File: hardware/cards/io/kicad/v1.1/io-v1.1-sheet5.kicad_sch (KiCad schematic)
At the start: 8 parts, among them IC10 74*273, IC5 74*138, IC7 74*00, IC8 74*06

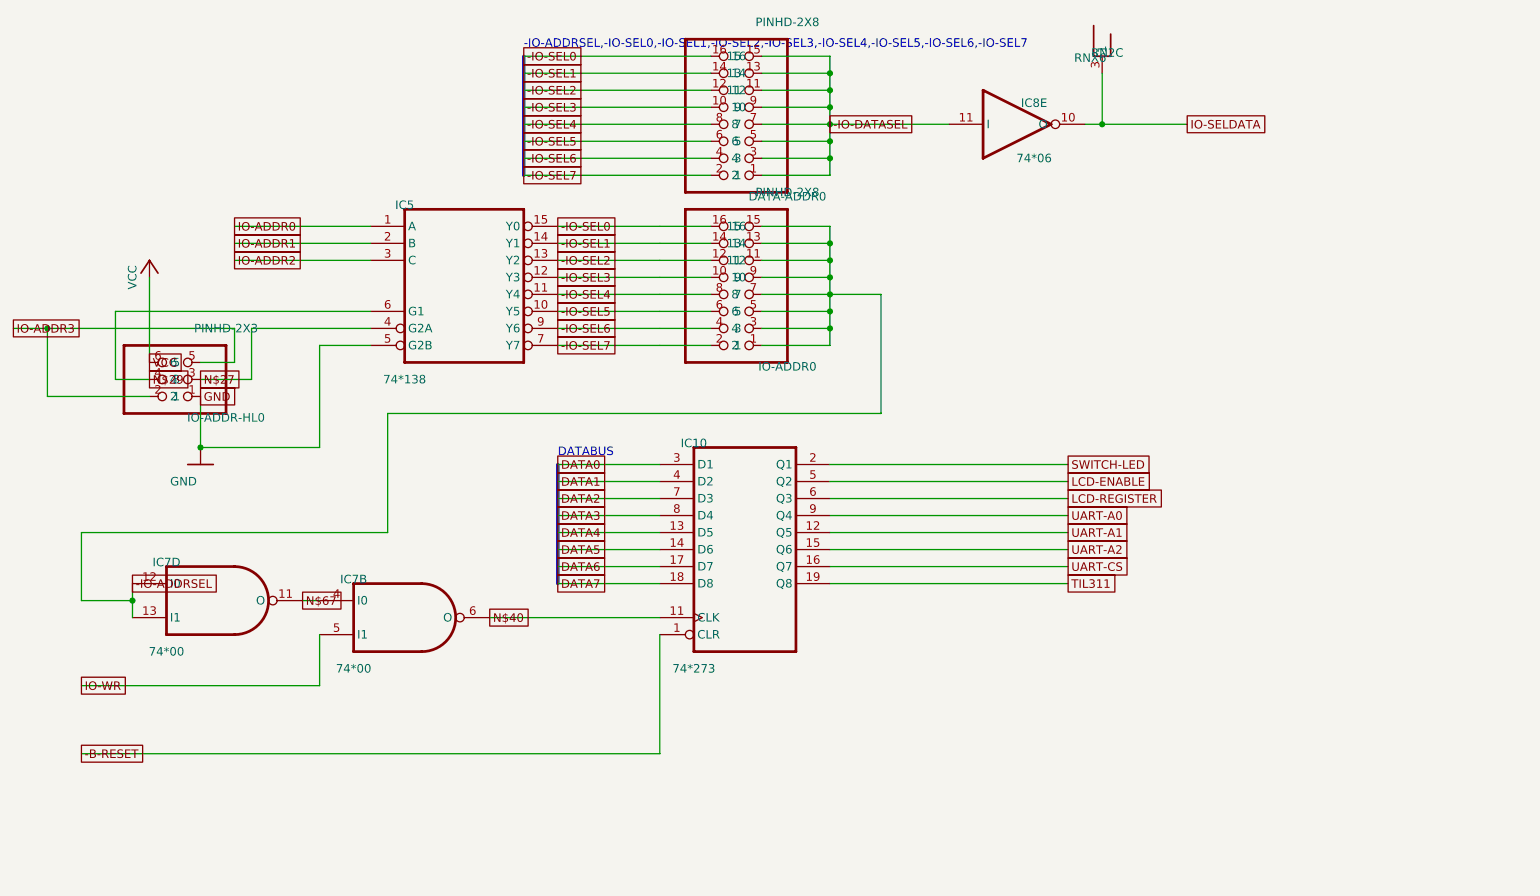
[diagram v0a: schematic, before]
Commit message: fix(kicad): readable converted schematics - overlaps 42,847 -> 3,147, nothing off the frame; CF sheet 0 overlaps
- tools/kicad/sch_overlaps.py: calibrated readability check (text/text, text/body, text/line, off frame/title block)
- eagle_sch_to_kicad.py: fields placed from Eagle's smashed attributes or the symbol's >NAME/>VALUE with Eagle's align,
  size and ratio, readable angles; fields Eagle never shows hidden (FABC96R shows only its pin name); pin numbers hidden
  where every Eagle pin hides them; Eagle-hidden layers dropped (the stray SpiceOrder text); labels on their own wires,
  converter labels only where KiCad needs them; rotate-then-mirror fixed for MR90/MR270 in pin_world/no-connects;
  each sheet on the smallest page that holds it, centred clear of the title block
- finish_board.py: stable footprint-library choice (DRC counts no longer vary run to run)
- all 37 projects regenerated: netlist proofs unchanged (34 MATCH, 2 schematic-only, video Fusion export MISMATCH as
  before); DRC same or better; ERC up (loose wire ends onto graphic buses no longer hidden by labels; explained per README)
- CF card: gate names off the gate bodies, U3 clear of its title, 5.08 mm connector pins; rebuilt: DRC 0/0, proof MATCH
- schematic PDFs regenerated (tools/sch_to_pdf.py, 37/37)

Co-Authored-By: Claude Opus 5.5 <noreply@anthropic.com>
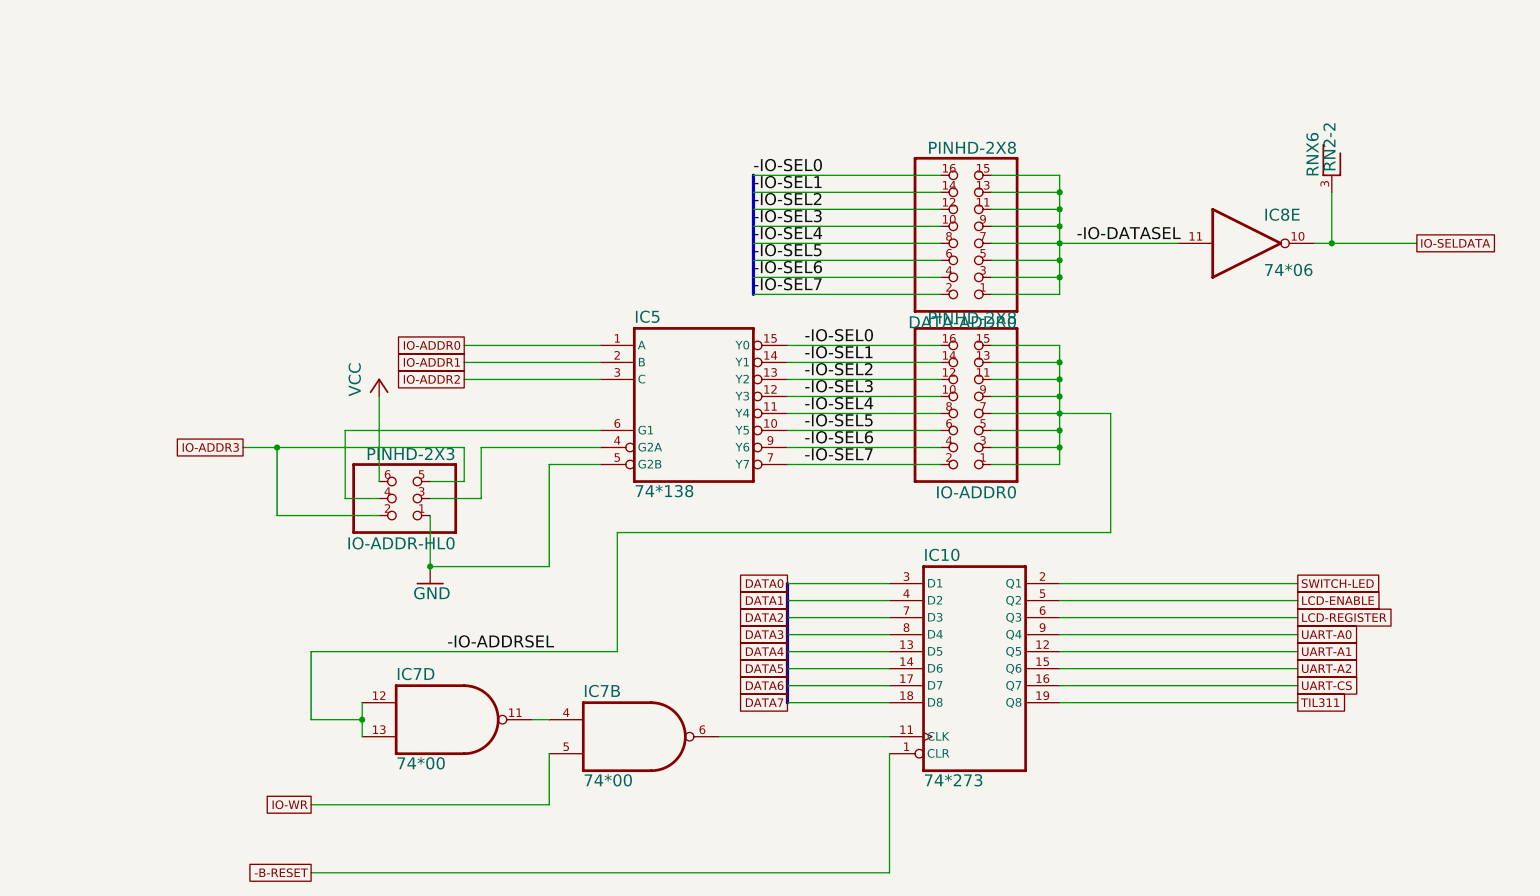
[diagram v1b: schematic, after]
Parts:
- RN2: Eagle name (none) -> RN2-2
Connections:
- net N$27: no longer names the net of IC5.4 (G2A), IO-ADDR-HL0.3
- net N$29: no longer names the net of IC5.6 (G1), IO-ADDR-HL0.4
- net N$40: no longer names the net of IC10.11 (CLK), IC7.6 (O)
- net N$67: no longer names the net of IC7.11 (O), IC7.4 (I0)
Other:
- note removed: "-IO-ADDRSEL,-IO-SEL0,-IO-SEL1,-IO-SEL2,-IO-SEL3,-IO-SEL4,-IO-SEL5,-IO-SEL6,-IO-SEL7"
- note removed: "DATABUS"
- moved on the sheet: IC10, IC5
